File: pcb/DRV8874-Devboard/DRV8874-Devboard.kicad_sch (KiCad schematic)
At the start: 56 parts, among them J1 Conn_01x04_Pin, J10 Conn_01x06_Pin, J12 Conn_01x03_Pin, J2 Screw_Terminal_01x02, J3 Conn_01x03_Pin, J4 Conn_01x03_Pin, J5 Conn_01x04_Pin, J6 Conn_01x03_Pin, J7 Conn_01x03_Pin, J8 Conn_01x03_Pin, J9 Conn_01x03_Pin, U1 DRV8874, U2 BL9342, U3 DRV8874, U4 SN65HVD230, U5 TPS16630PWPR, U6 M95320-WMN6TP, U7 TinyThinker_J1

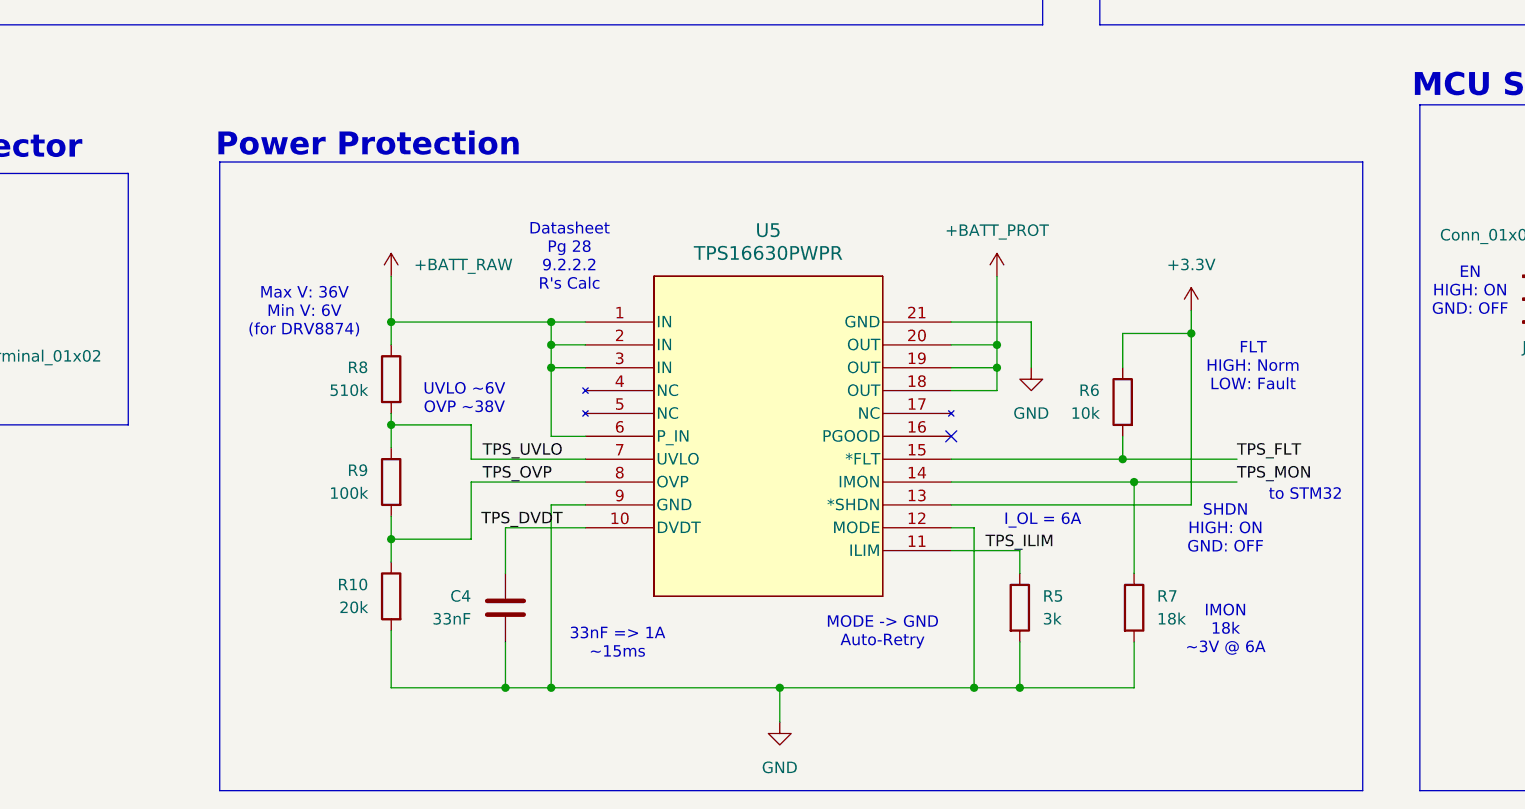
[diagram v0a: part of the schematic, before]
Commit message: finished rough routing of DRV8874
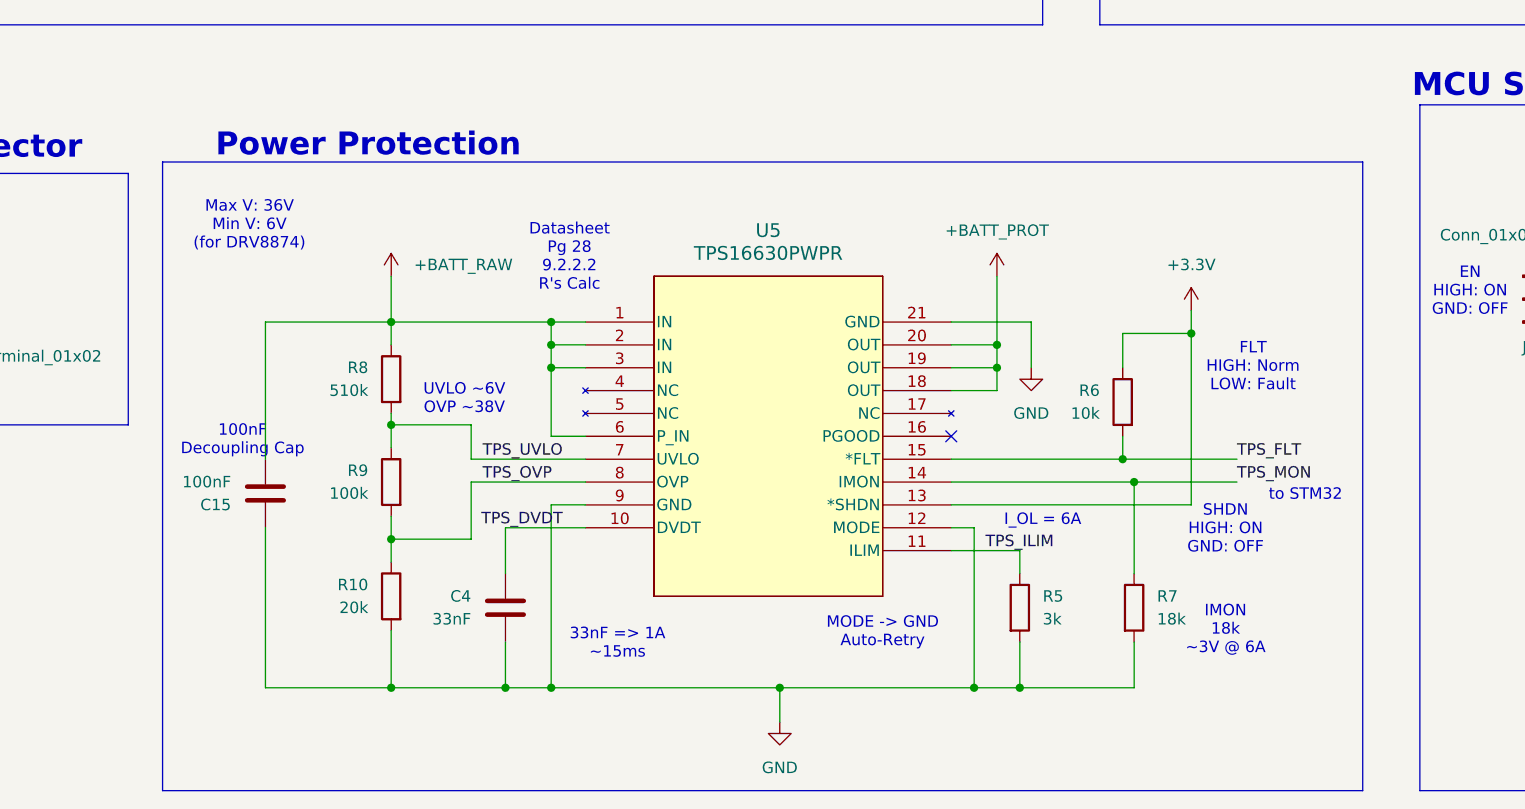
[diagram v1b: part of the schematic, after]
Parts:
- added C15: 100nF, Capacitor_SMD:C_0402_1005Metric, symbol Device:C
- U5: footprint Package_SO:HTSSOP-20-1EP_4.4x6.5mm_P0.65mm_EP2.85x4mm -> HTSSOP20_PWP_TEX
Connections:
- net +BATT_RAW: now also C15.2
- net GND: now also C15.1
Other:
- note added: "100nF Decoupling Cap"
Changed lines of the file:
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@@
 	)
 	(rectangle
-		(start 73.66 242.57)
+		(start 67.31 242.57)
 		(end 200.66 312.42)
 		(stroke
@@
 		)
 	)
+	(text "100nF \nDecoupling Cap\n"
+		(exclude_from_sim no)
+		(at 76.2 273.558 0)
+		(effects
+			(font
+				(size 1.27 1.27)
+			)
+		)
+	)
 	(text "HOLD\nHIGH -> Unused\nLOW -> SPI Paused"
 		(exclude_from_sim no)
@@
 	(text "Max V: 36V\nMin V: 6V\n(for DRV8874)"
 		(exclude_from_sim no)
-		(at 83.058 259.334 0)
+		(at 76.962 249.682 0)
 		(effects
 			(font
@@
 	)
 	(junction
+		(at 92.71 300.99)
+		(diameter 0)
+		(color 0 0 0 0)
+	)
+	(junction
 		(at 314.96 254)
 		(diameter 0)
@@
 	(wire
 		(pts
+			(xy 78.74 283.21) (xy 78.74 300.99)
+		)
+		(stroke
+			(width 0)
+			(type default)
+		)
+	)
+	(wire
+		(pts
 			(xy 106.68 115.57) (xy 114.3 115.57)
 		)
@@
 	(wire
 		(pts
+			(xy 78.74 260.35) (xy 78.74 275.59)
+		)
+		(stroke
+			(width 0)
+			(type default)
+		)
+	)
+	(wire
+		(pts
 			(xy 271.78 251.46) (xy 271.78 254)
 		)
@@
 	(wire
 		(pts
+			(xy 78.74 300.99) (xy 92.71 300.99)
+		)
+		(stroke
+			(width 0)
+			(type default)
+		)
+	)
+	(wire
+		(pts
 			(xy 283.21 88.9) (xy 283.21 97.79)
 		)
@@
 	(wire
 		(pts
+			(xy 92.71 260.35) (xy 78.74 260.35)
+		)
+		(stroke
+			(width 0)
+			(type default)
+		)
+	)
+	(wire
+		(pts
 			(xy 278.13 66.04) (xy 278.13 50.8)
 		)
@@
 			)
 		)
-		(property "Footprint" "Package_SO:HTSSOP-20-1EP_4.4x6.5mm_P0.65mm_EP2.85x4mm"
+		(property "Footprint" "HTSSOP20_PWP_TEX"
 			(at 114.3 260.35 0)
 			(effects
@@
 					(unit 1)
 				)
+			)
+		)
+	)
+	(symbol
+		(lib_id "Device:C")
+		(at 78.74 279.4 180)
+		(unit 1)
+		(exclude_from_sim no)
+		(in_bom yes)
+		(on_board yes)
+		(dnp no)
+		(property "Reference" "C15"
+			(at 74.93 280.6701 0)
+			(effects
+				(font
+					(size 1.27 1.27)
+				)
+				(justify left)
+			)
+		)
+		(property "Value" "100nF"
+			(at 74.93 278.1301 0)
+			(effects
+				(font
+					(size 1.27 1.27)
+				)
+				(justify left)
+			)
+		)
+		(property "Footprint" "Capacitor_SMD:C_0402_1005Metric"
+			(at 77.7748 275.59 0)
+			(effects
+				(font
+					(size 1.27 1.27)
+				)
+				(hide yes)
+			)
+		)
+		(property "Datasheet" "~"
+			(at 78.74 279.4 0)
+			(effects
+				(font
+					(size 1.27 1.27)
+				)
+				(hide yes)
+			)
+		)
+		(property "Description" "Unpolarized capacitor"
+			(at 78.74 279.4 0)
+			(effects
+				(font
+					(size 1.27 1.27)
+				)
+				(hide yes)
+			)
+		)
+		(property "JLCPCB Part #" " C307331"
+			(at 78.74 279.4 0)
+			(effects
+				(font
+					(size 1.27 1.27)
+				)
+				(hide yes)
+			)
+		)
+		(property "Sim.Device" ""
+			(at 78.74 279.4 0)
+			(effects
+				(font
+					(size 1.27 1.27)
+				)
+				(hide yes)
+			)
+		)
+		(property "Sim.Pins" ""
+			(at 78.74 279.4 0)
+			(effects
+				(font
+					(size 1.27 1.27)
+				)
+				(hide yes)
+			)
+		)
+		(property "Sim.Type" ""
+			(at 78.74 279.4 0)
+			(effects
+				(font
+					(size 1.27 1.27)
+				)
+				(hide yes)
+			)
+		)
+		(property "FT Rotation Offset" ""
+			(at 78.74 279.4 0)
+			(effects
+				(font
+					(size 1.27 1.27)
+				)
+				(hide yes)
+			)
+		)
+		(property "FT Position Offset" ""
+			(at 78.74 279.4 0)
+			(effects
+				(font
+					(size 1.27 1.27)
+				)
+				(hide yes)
+			)
+		)
+		(pin "1"
+		)
+		(pin "2"
+		)
+		(instances
+			(project "DRV8874-Devboard"
+				(path "/b57ce88b-13b6-41b4-aa44-cbc2ef4083a9"
+					(reference "C15")
+					(unit 1)
+				)

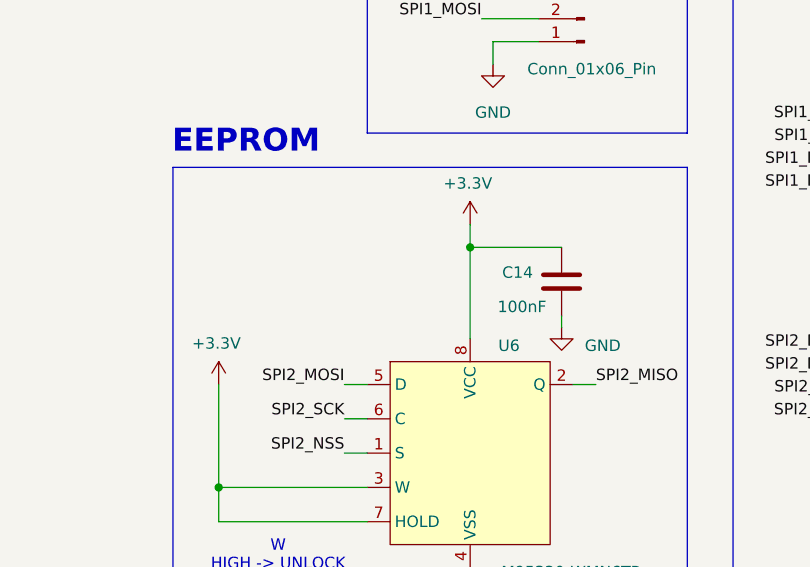
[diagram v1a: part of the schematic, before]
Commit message: finished rough layout of EEPROM
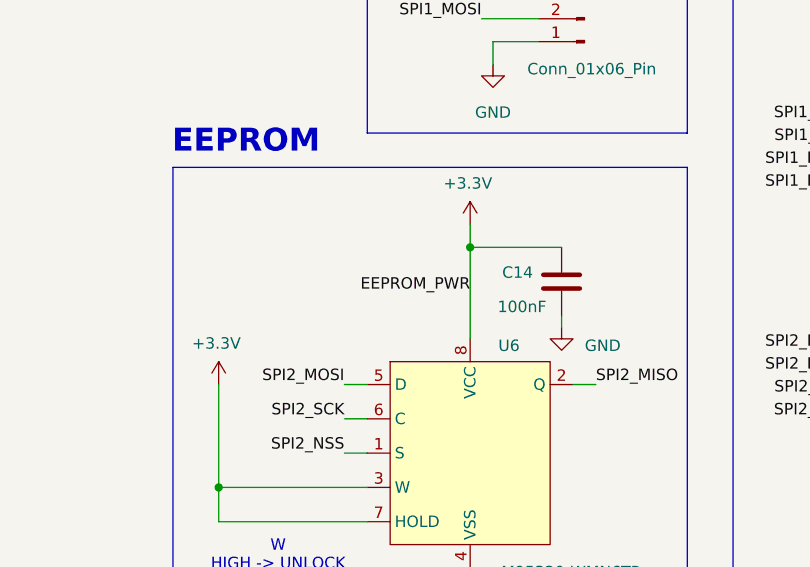
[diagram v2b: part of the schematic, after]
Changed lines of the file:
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@@
+		)
+	)
+	(label "EEPROM_PWR"
+		(at 231.14 72.39 180)
+		(effects
+			(font
+				(size 1.27 1.27)
+			)
+			(justify right bottom)
 		)
 	)

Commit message: more minor routing cleanup
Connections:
- net A_IN1: now also U7.12 (TIM3_CH1); no longer U7.32 (TIM2_CH1)
- net A_IN2: now also U7.9 (TIM3_CH2); no longer U7.29 (TIM2_CH4)
- net B_IN1: now also U7.8 (TIM3_CH3); no longer U7.36 (TIM2_CH3)
- net B_IN2: now also U7.5 (TIM3_CH4); no longer U7.33 (TIM2_CH2)
- no-connect marks 17 -> 13
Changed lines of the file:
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@@
 	)
 	(no_connect
-		(at 372.11 53.34)
-	)
-	(no_connect
 		(at 400.05 91.44)
 	)
@@
 	)
 	(no_connect
-		(at 372.11 48.26)
-	)
-	(no_connect
-		(at 400.05 55.88)
-	)
-	(no_connect
-		(at 400.05 50.8)
-	)
-	(no_connect
 		(at 372.11 45.72)
 	)
@@
 	)
 	(label "B_IN2"
-		(at 372.11 83.82 180)
+		(at 372.11 48.26 180)
 		(effects
 			(font
@@
 	)
 	(label "A_IN2"
-		(at 372.11 78.74 180)
+		(at 372.11 53.34 180)
 		(effects
 			(font
@@
 	)
 	(label "A_IN1"
-		(at 400.05 81.28 0)
+		(at 400.05 55.88 0)
 		(effects
 			(font
@@
 	)
 	(label "B_IN1"
-		(at 400.05 86.36 0)
+		(at 400.05 50.8 0)
 		(effects
 			(font

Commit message: added 4 WS2812B RGB LEDs for status codes
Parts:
- added D1, D3, D4, D5: WS2812B-2020, LED_SMD:LED_WS2812B-2020_PLCC4_2.0x2.0mm, symbol LED:WS2812B-2020
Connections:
- net ADC_VSENSE: now also U7.21 (ADC1_IN15); no longer U7.20 (ADC1_IN8)
- net A_IPROPI: now also U7.20 (ADC1_IN8); no longer U7.21 (ADC1_IN15)
- net GND: now also D1.2 (VSS), D3.2 (VSS), D4.2 (VSS), D5.2 (VSS)
- net +5V_SYS: now reaches U7.3 (+5V_SYS)
- net +5V_SYS: now also D1.4 (VDD), D3.4 (VDD), D4.4 (VDD), D5.4 (VDD)
- net RGB_LED_PWM: now reaches U7.32 (TIM2_CH1)
- net RGB_LED_PWM: now also D1.3 (DIN)
- net +5V renamed +5V_EXT
- new net: D3.3 (DIN), D4.1 (DOUT)
- new net: D4.3 (DIN), D5.1 (DOUT)
- new net: D1.1 (DOUT), D5.3 (DIN)

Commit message: added connector for SWD
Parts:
- added J11: Conn_01x06_Pin, Connector_PinHeader_2.54mm:PinHeader_1x06_P2.54mm_Vertical, symbol Connector:Conn_01x06_Pin
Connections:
- net +3.3V: now also J11.2 (Pin_2), J11.6 (Pin_6)
- net GND: now also J11.3 (Pin_3)
- net NRST: now reaches U7.40 (NRST)
- net NRST: now also J11.1 (Pin_1)
- net SWDIO: now reaches U7.44 (SWDIO)
- net SWDIO: now also J11.5 (Pin_5)
- net SWCLK: now reaches U7.46 (SWCLK)
- net SWCLK: now also J11.4 (Pin_4)
- no-connect marks 13 -> 10

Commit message: switched WorldSemi WS2812B to XingLight
WorldSemi is only for Standard PCBA plus it needs baking. XingLight needs capacitors and resistors though
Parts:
- added C16, C17, C18, C19: 100nF, Capacitor_SMD:C_0402_1005Metric, symbol Device:C
- added R23: 470, Resistor_SMD:R_0402_1005Metric, symbol Device:R
- D1, D3, D4, D5: JLCPCB Part # C52917434 -> C3646929
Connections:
- net +5V_SYS: now also C16.1, C17.1, C18.1, C19.1
- net GND: now also C16.2, C17.2, C18.2, C19.2
- net RGB_LED_PWM: now also U7.33 (TIM2_CH2), R23.1; no longer D1.3 (DIN), U7.32 (TIM2_CH1)
- new net: D1.3 (DIN), R23.2
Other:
- note added: "500 ohm recommended 470 is closest on JLC Basic"
- moved on the sheet: D3, D4, D5, J11

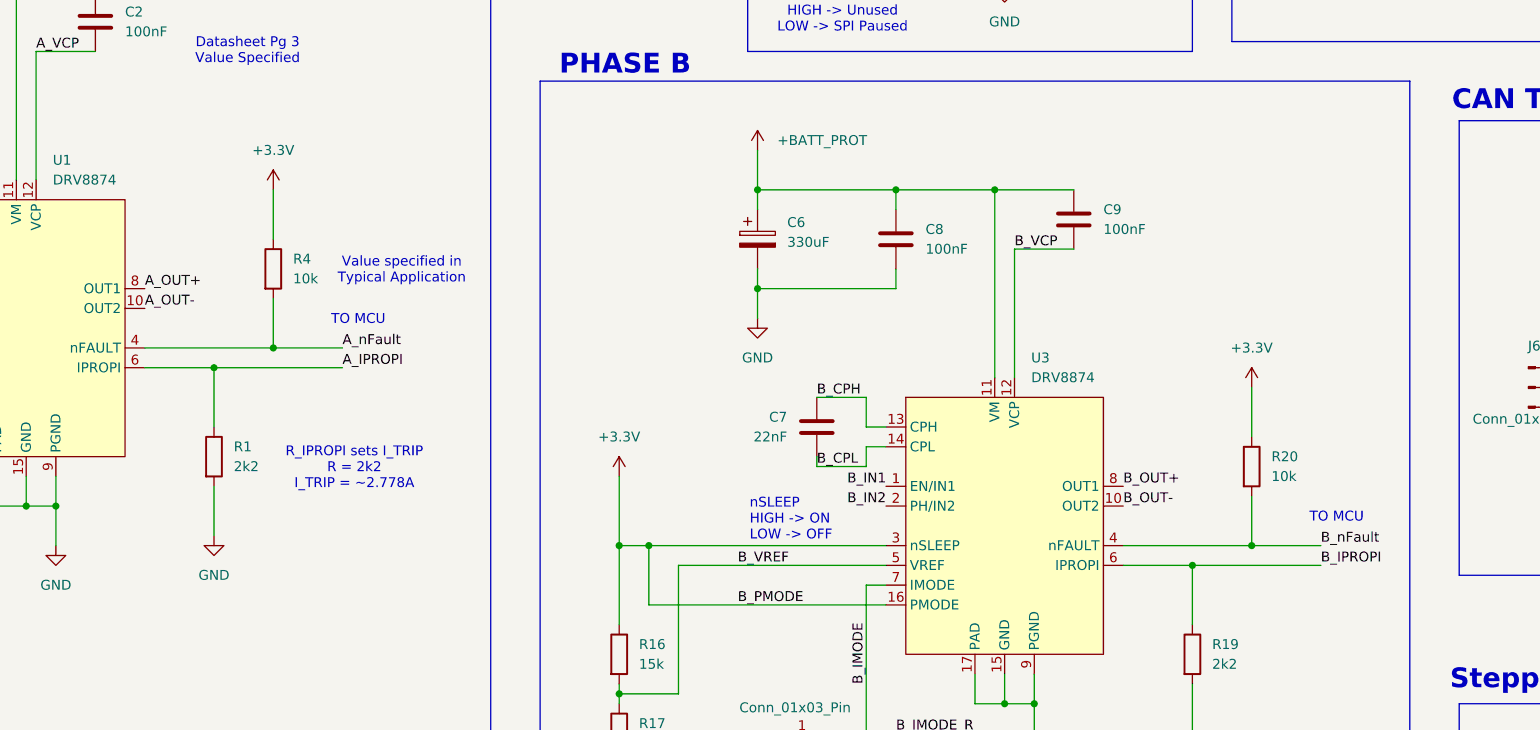
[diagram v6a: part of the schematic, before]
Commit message: added stitching vias
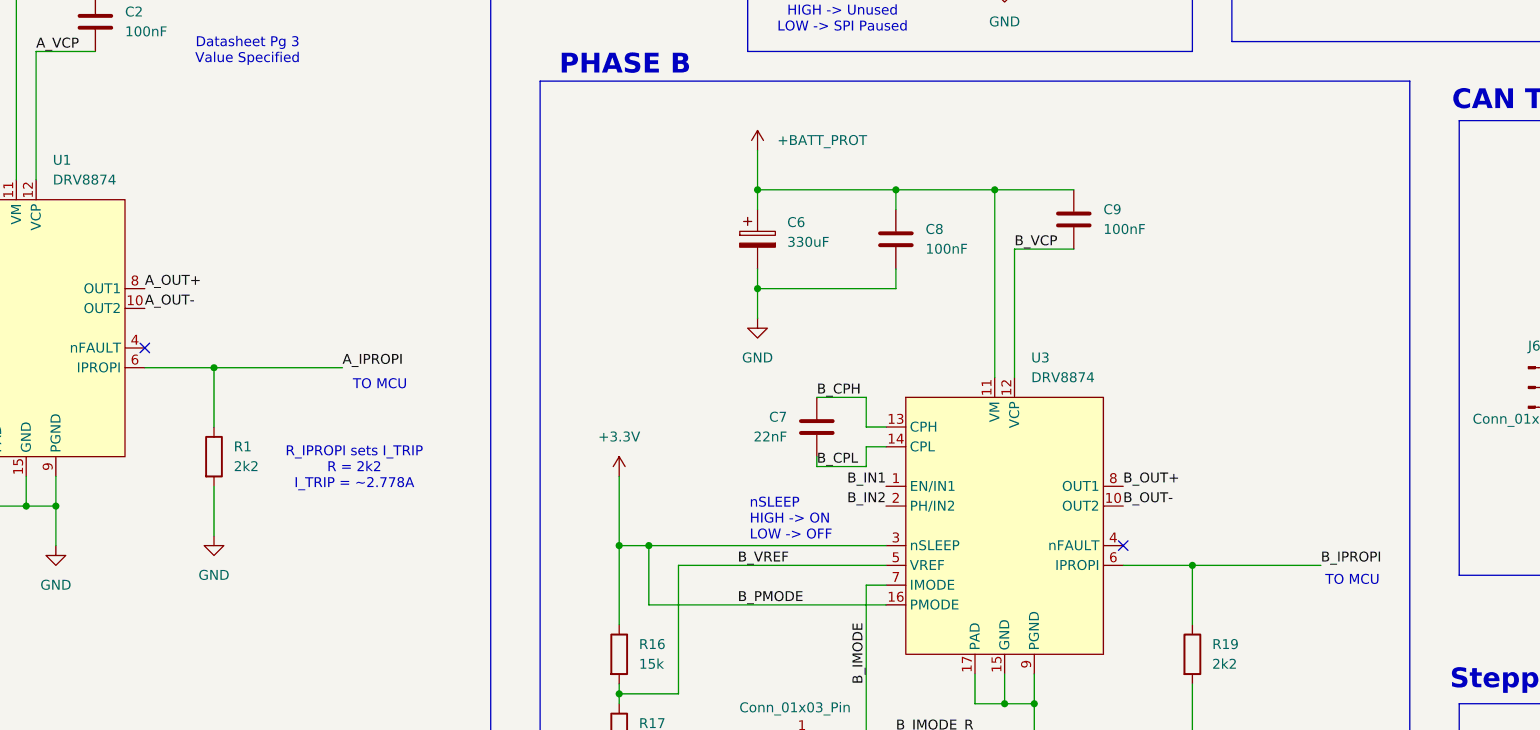
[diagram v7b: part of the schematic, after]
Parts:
- removed R20, R4: 10k, Resistor_SMD:R_0402_1005Metric, symbol Device:R
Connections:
- net A_nFault: no longer names the net of U1.4 (nFAULT)
- net B_nFault: no longer names the net of U3.4 (nFAULT)
- no-connect marks 10 -> 12
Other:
- note removed: "Value specified in Typical Application"

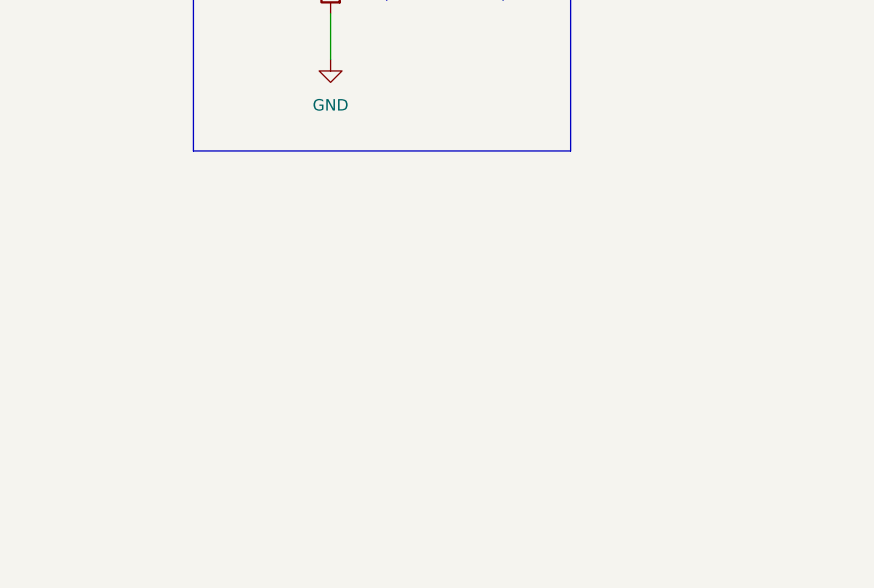
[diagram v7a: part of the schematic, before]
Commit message: added pins to expose 5v and batt_prot
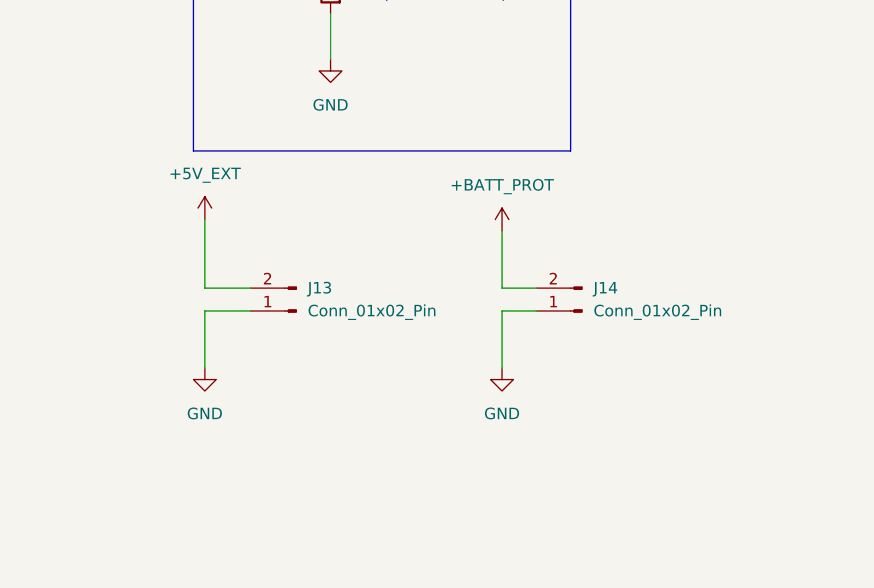
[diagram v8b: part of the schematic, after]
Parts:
- added J13, J14: Conn_01x02_Pin, Connector_PinHeader_2.54mm:PinHeader_1x02_P2.54mm_Vertical, symbol Connector:Conn_01x02_Pin
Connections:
- net +5V_EXT: now also J13.2 (Pin_2)
- net +BATT_PROT: now also J14.2 (Pin_2)
- net GND: now also J13.1 (Pin_1), J14.1 (Pin_1)
